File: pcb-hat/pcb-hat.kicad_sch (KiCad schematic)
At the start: 42 parts, among them U1 INA219AxD, U2 AOZ6605PI-1, U3 HTD Servo, U4 Vertical_Pi_Breakout, U5 Raspberry_Pi_Generic, U6 Power_Connector, U7 LM1084ISX-5.0_NOPB, U8 Horizontal_Pi_Breakout

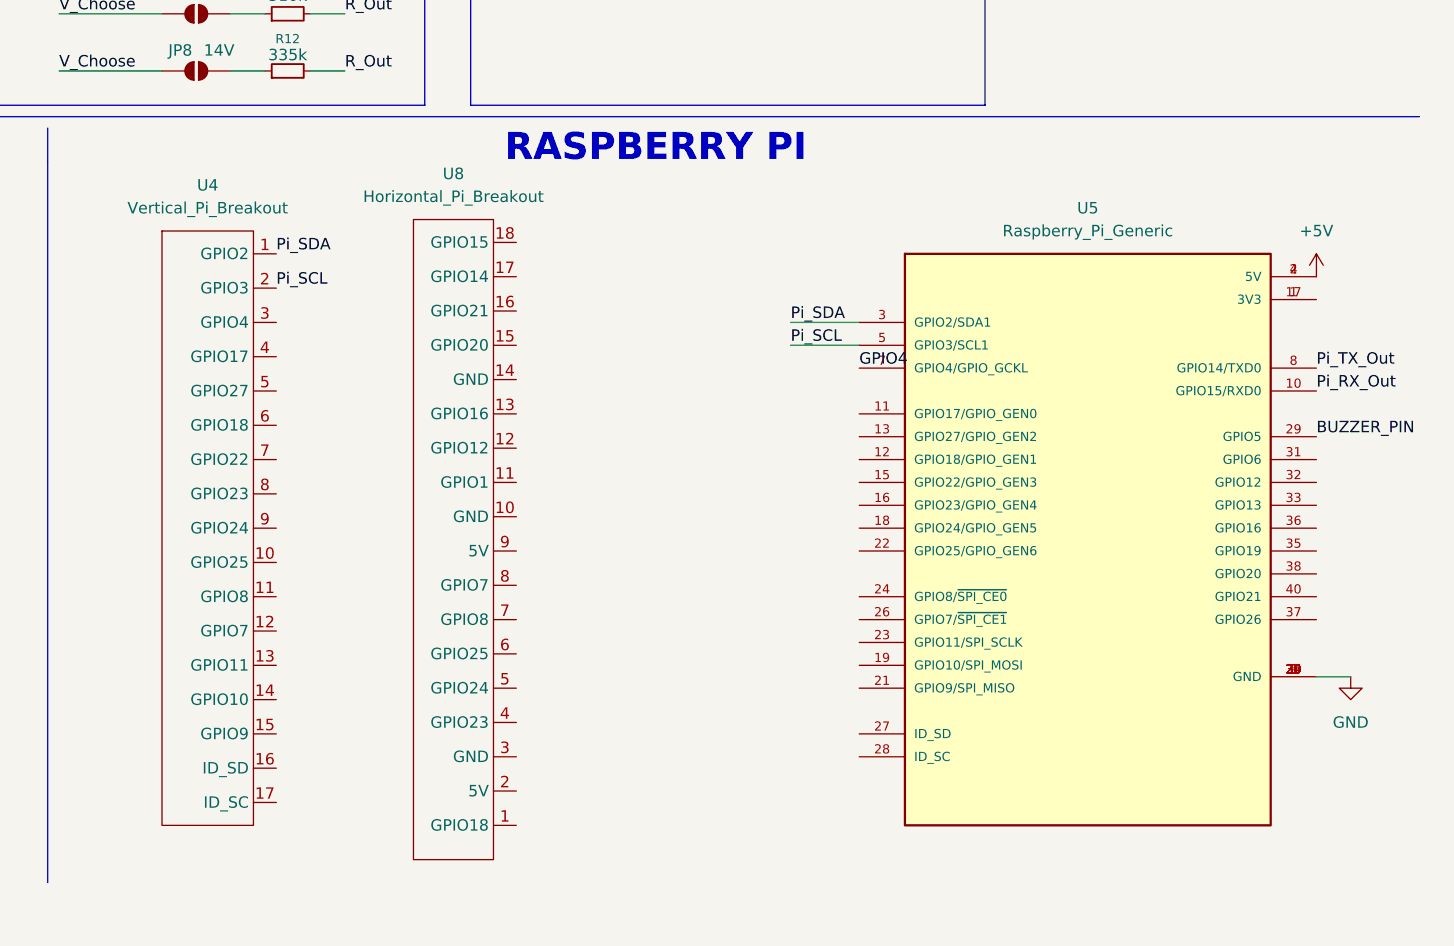
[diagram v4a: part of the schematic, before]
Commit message: symbol/footprint/connections for PiHeaders/pinouts
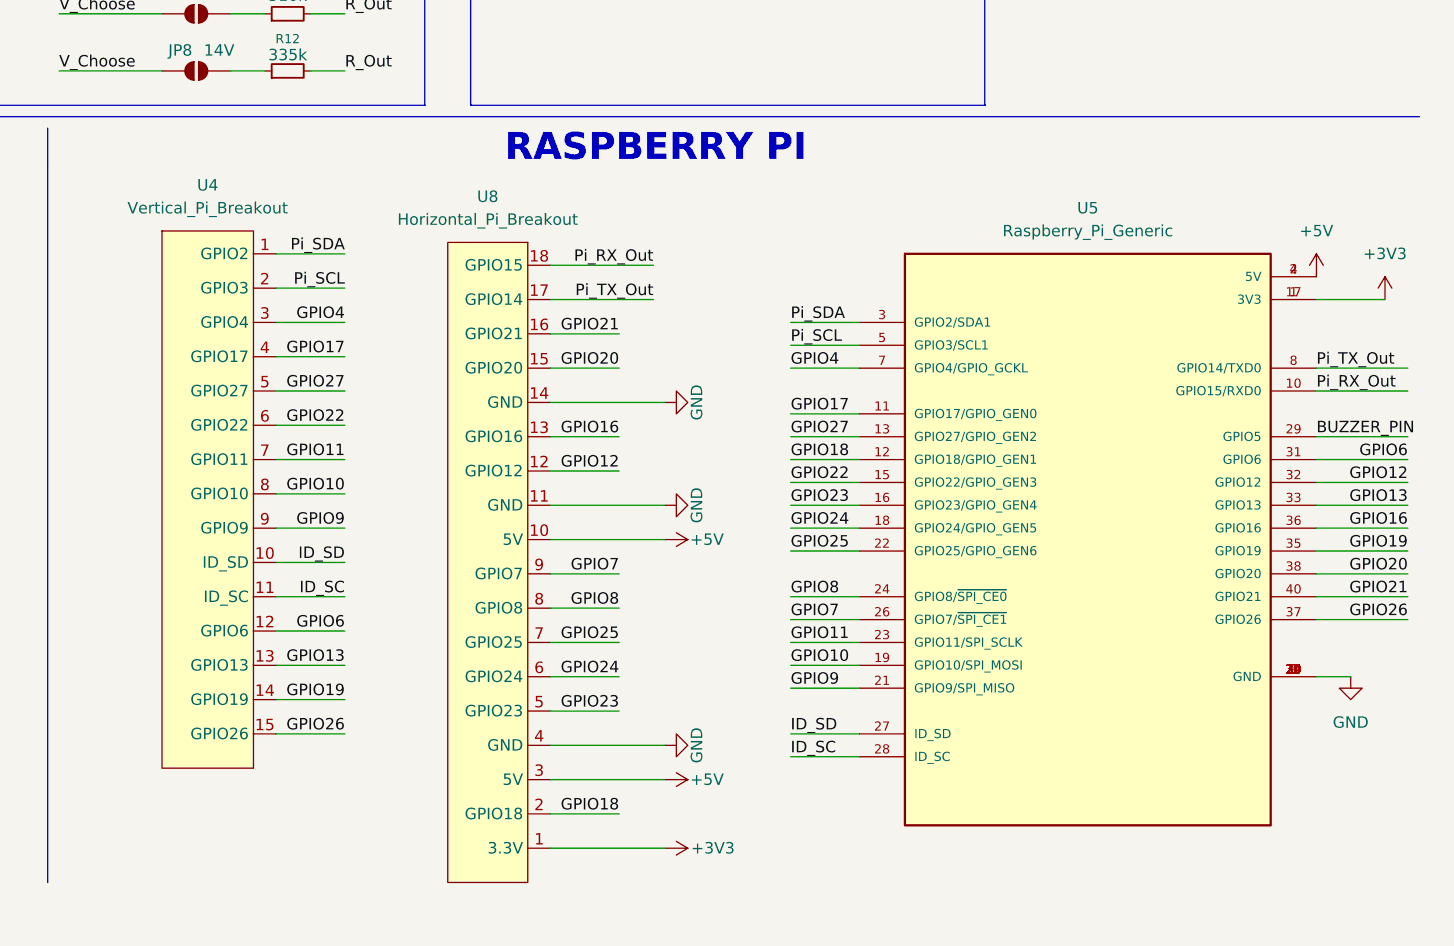
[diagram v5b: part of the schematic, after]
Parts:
- U4: footprint (none) -> Connector_PinHeader_2.54mm:PinHeader_1x15_P2.54mm_Vertical
- U8: footprint (none) -> Connector_PinHeader_2.54mm:PinHeader_1x18_P2.54mm_Vertical
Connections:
- net +5V: now also U8.10 (5V), U8.3 (5V)
- net GND: now also U5.14 (GND), U8.11 (GND), U8.14 (GND), U8.4 (GND)
- net GPIO4: now also U4.3 (GPIO4)
- net Pi_RX_Out: now also U8.18 (GPIO15)
- net Pi_TX_Out: now also U8.17 (GPIO14)
- net +3V3: now reaches U5.1 (3V3), U5.17 (3V3)
- net +3V3: now also U8.1 (3.3V)
- net GPIO17: now reaches U5.11 (GPIO17/GPIO_GEN0)
- net GPIO17: now also U4.4 (GPIO17)
- net GPIO18: now reaches U5.12 (GPIO18/GPIO_GEN1)
- net GPIO18: now also U8.2 (GPIO18)
- net GPIO27: now reaches U5.13 (GPIO27/GPIO_GEN2)
- net GPIO27: now also U4.5 (GPIO27)
- net GPIO22: now reaches U5.15 (GPIO22/GPIO_GEN3)
- net GPIO22: now also U4.6 (GPIO22)
- net GPIO23: now reaches U5.16 (GPIO23/GPIO_GEN4)
- net GPIO23: now also U8.5 (GPIO23)
- net GPIO24: now reaches U5.18 (GPIO24/GPIO_GEN5)
- net GPIO24: now also U8.6 (GPIO24)
- net GPIO10: now reaches U5.19 (GPIO10/SPI_MOSI)
- net GPIO10: now also U4.8 (GPIO10)
- net GPIO9: now reaches U5.21 (GPIO9/SPI_MISO)
- net GPIO9: now also U4.9 (GPIO9)
- net GPIO25: now reaches U5.22 (GPIO25/GPIO_GEN6)
- net GPIO25: now also U8.7 (GPIO25)
- net GPIO11: now reaches U5.23 (GPIO11/SPI_SCLK)
- net GPIO11: now also U4.7 (GPIO11)
- net GPIO8: now reaches U5.24 (GPIO8/~{SPI_CE0})
- net GPIO8: now also U8.8 (GPIO8)
- net GPIO7: now reaches U5.26 (GPIO7/~{SPI_CE1})
- net GPIO7: now also U8.9 (GPIO7)
- net ID_SD: now reaches U5.27 (ID_SD)
- net ID_SD: now also U4.10 (ID_SD)
- net ID_SC: now reaches U5.28 (ID_SC)
- net ID_SC: now also U4.11 (ID_SC)
- net GPIO6: now reaches U5.31 (GPIO6)
- net GPIO6: now also U4.12 (GPIO6)
- net GPIO12: now reaches U5.32 (GPIO12)
- net GPIO12: now also U8.12 (GPIO12)
- net GPIO13: now reaches U5.33 (GPIO13)
- net GPIO13: now also U4.13 (GPIO13)
- net GPIO19: now reaches U5.35 (GPIO19)
- net GPIO19: now also U4.14 (GPIO19)
- net GPIO16: now reaches U5.36 (GPIO16)
- net GPIO16: now also U8.13 (GPIO16)
- net GPIO26: now reaches U5.37 (GPIO26)
- net GPIO26: now also U4.15 (GPIO26)
- net GPIO20: now reaches U5.38 (GPIO20)
- net GPIO20: now also U8.15 (GPIO20)
- net GPIO21: now reaches U5.40 (GPIO21)
- net GPIO21: now also U8.16 (GPIO21)

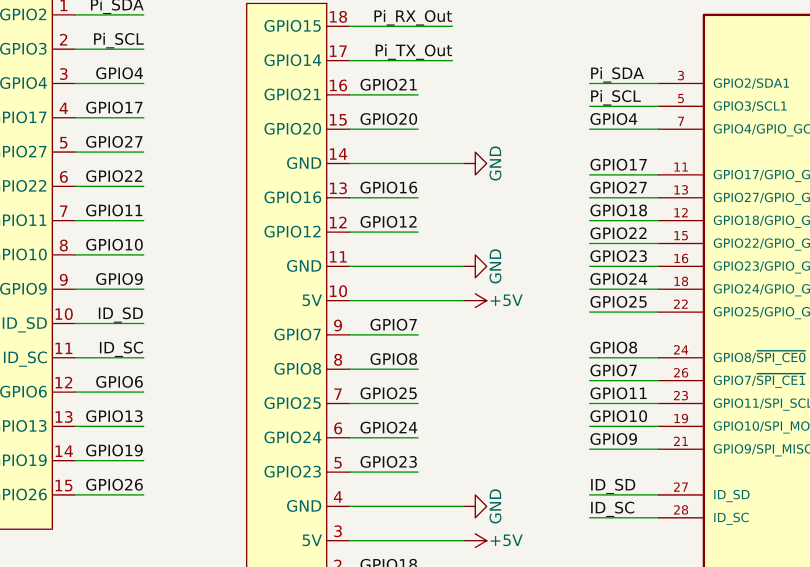
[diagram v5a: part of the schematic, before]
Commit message: pi breakout symbol changes
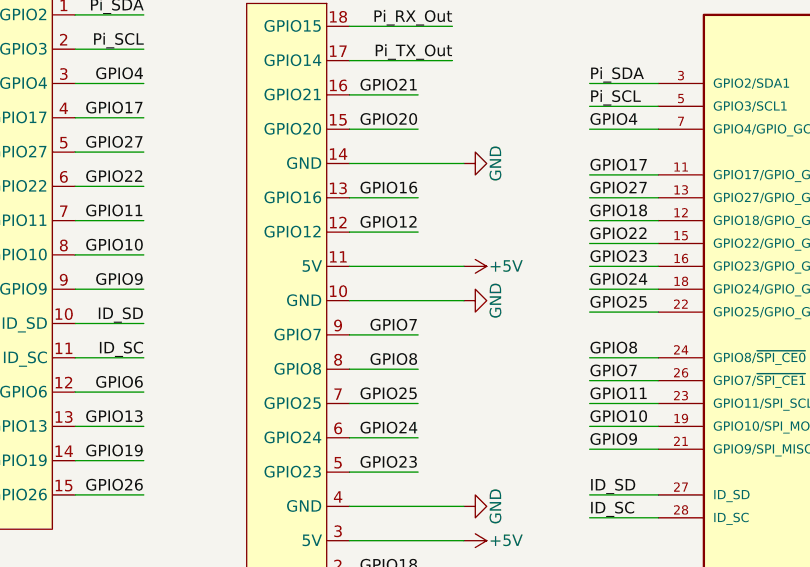
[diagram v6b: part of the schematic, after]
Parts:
- U8: footprint Connector_PinHeader_2.54mm:PinHeader_1x18_P2.54mm_Vertical -> (none)
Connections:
- net +5V: now also U8.11 (5V); no longer U8.10 (5V)
- net GND: now also U8.10 (GND); no longer U8.11 (GND)
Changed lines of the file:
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@@
 	(wire
 		(pts
-			(xy 185.42 125.73) (xy 198.12 125.73)
+			(xy 185.42 121.92) (xy 198.12 121.92)
 		)
 		(stroke
@@
 	(wire
 		(pts
-			(xy 185.42 121.92) (xy 198.12 121.92)
+			(xy 185.42 125.73) (xy 198.12 125.73)
 		)
 		(stroke
@@
 	)
 	(symbol
+		(lib_id "PiHatComponents:horizontal_pi_breakout")
+		(at 201.93 128.27 270)
+		(unit 1)
+		(exclude_from_sim no)
+		(in_bom yes)
+		(on_board yes)
+		(dnp no)
+		(fields_autoplaced yes)
+		(property "Reference" "U8"
+			(at 178.435 87.63 90)
+			(effects
+				(font
+					(size 1.27 1.27)
+				)
+			)
+		)
+		(property "Value" "Horizontal_Pi_Breakout"
+			(at 178.435 90.17 90)
+			(effects
+				(font
+					(size 1.27 1.27)
+				)
+			)
+		)
+		(property "Footprint" ""
+			(at 201.93 128.27 0)
+			(effects
+				(font
+					(size 1.27 1.27)
+				)
+				(hide yes)
+			)
+		)
+		(property "Datasheet" ""
+			(at 201.93 128.27 0)
+			(effects
+				(font
+					(size 1.27 1.27)
+				)
+				(hide yes)
+			)
+		)
+		(property "Description" ""
+			(at 201.93 128.27 0)
+			(effects
+				(font
+					(size 1.27 1.27)
+				)
+				(hide yes)
+			)
+		)
+		(pin "14"
+		)
+		(pin "12"
+		)
+		(pin "8"
+		)
+		(pin "16"
+		)
+		(pin "18"
+		)
+		(pin "17"
+		)
+		(pin "15"
+		)
+		(pin "13"
+		)
+		(pin "10"
+		)
+		(pin "9"
+		)
+		(pin "11"
+		)
+		(pin "5"
+		)
+		(pin "7"
+		)
+		(pin "1"
+		)
+		(pin "6"
+		)
+		(pin "4"
+		)
+		(pin "3"
+		)
+		(pin "2"
+		)
+		(instances
+			(project ""
+				(path "/a3c2d30d-0751-4de7-a899-3d89ad40795d"
+					(reference "U8")
+					(unit 1)
+				)
+			)
+		)
+	)
+	(symbol
 		(lib_id "Device:C_Small")
 		(at 223.52 49.53 0)
@@
 	(symbol
 		(lib_id "power:+5V")
-		(at 198.12 125.73 270)
+		(at 198.12 121.92 270)
 		(unit 1)
 		(exclude_from_sim no)
@@
 		(dnp no)
 		(property "Reference" "#PWR032"
-			(at 194.31 125.73 0)
+			(at 194.31 121.92 0)
 			(effects
 				(font
@@
 		)
 		(property "Value" "+5V"
-			(at 200.914 125.73 90)
+			(at 200.914 121.92 90)
 			(effects
 				(font
@@
 		)
 		(property "Footprint" ""
-			(at 198.12 125.73 0)
+			(at 198.12 121.92 0)
 			(effects
 				(font
@@
 		)
 		(property "Datasheet" ""
-			(at 198.12 125.73 0)
+			(at 198.12 121.92 0)
 			(effects
 				(font
@@
 		)
 		(property "Description" "Power symbol creates a global label with name \"+5V\""
-			(at 198.12 125.73 0)
+			(at 198.12 121.92 0)
 			(effects
 				(font
@@
 	(symbol
 		(lib_id "power:GND")
-		(at 198.12 121.92 90)
+		(at 198.12 125.73 90)
 		(unit 1)
 		(exclude_from_sim no)
@@
 		(dnp no)
 		(property "Reference" "#PWR030"
-			(at 204.47 121.92 0)
+			(at 204.47 125.73 0)
 			(effects
 				(font
@@
 		)
 		(property "Value" "GND"
-			(at 201.676 121.92 0)
+			(at 201.676 125.73 0)
 			(effects
 				(font
@@
 		)
 		(property "Footprint" ""
-			(at 198.12 121.92 0)
+			(at 198.12 125.73 0)
 			(effects
 				(font
@@
 		)
 		(property "Datasheet" ""
-			(at 198.12 121.92 0)
+			(at 198.12 125.73 0)
 			(effects
 				(font
@@
 		)
 		(property "Description" "Power symbol creates a global label with name \"GND\" , ground"
-			(at 198.12 121.92 0)
+			(at 198.12 125.73 0)
 			(effects
 				(font
@@
 					(unit 1)
 				)
-			)
-		)
-	)
-	(symbol
-		(lib_id "PiHatComponents:horizontal_pi_breakout")
-		(at 201.93 128.27 270)
-		(unit 1)
-		(exclude_from_sim no)
-		(in_bom yes)
-		(on_board yes)
-		(dnp no)
-		(fields_autoplaced yes)
-		(property "Reference" "U8"
-			(at 178.435 87.63 90)
-			(effects
-				(font
-					(size 1.27 1.27)
-				)
-			)
-		)
-		(property "Value" "Horizontal_Pi_Breakout"
-			(at 178.435 90.17 90)
-			(effects
-				(font
-					(size 1.27 1.27)
-				)
-			)
-		)
-		(property "Footprint" "Connector_PinHeader_2.54mm:PinHeader_1x18_P2.54mm_Vertical"
-			(at 201.93 128.27 0)
-			(effects
-				(font
-					(size 1.27 1.27)
-				)
-				(hide yes)
-			)
-		)
-		(property "Datasheet" ""
-			(at 201.93 128.27 0)
-			(effects
-				(font
-					(size 1.27 1.27)
-				)
-				(hide yes)
-			)
-		)
-		(property "Description" ""
-			(at 201.93 128.27 0)
-			(effects
-				(font
-					(size 1.27 1.27)
-				)
-				(hide yes)
-			)
-		)
-		(pin "14"
-		)
-		(pin "10"
-		)
-		(pin "13"
-		)
-		(pin "4"
-		)
-		(pin "3"
-		)
-		(pin "5"
-		)
-		(pin "9"
-		)
-		(pin "11"
-		)
-		(pin "1"
-		)
-		(pin "16"
-		)
-		(pin "12"
-		)
-		(pin "6"
-		)
-		(pin "17"
-		)
-		(pin "18"
-		)
-		(pin "15"
-		)
-		(pin "8"
-		)
-		(pin "7"
-		)
-		(pin "2"
-		)
-		(instances
-			(project ""
-				(path "/a3c2d30d-0751-4de7-a899-3d89ad40795d"
-					(reference "U8")
-					(unit 1)
-				)
